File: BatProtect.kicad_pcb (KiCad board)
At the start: 2 copper layers, 94.5 x 100 mm, 57 parts, among them J1 PC104, J13 Charge3+, J16 uInv2+, J17 uInv1+, J19 uInv3+, J2 VBat1+, J3 BCharge1+, J4 BCharge3+, J5 Charge1+, J7 BCharge2+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

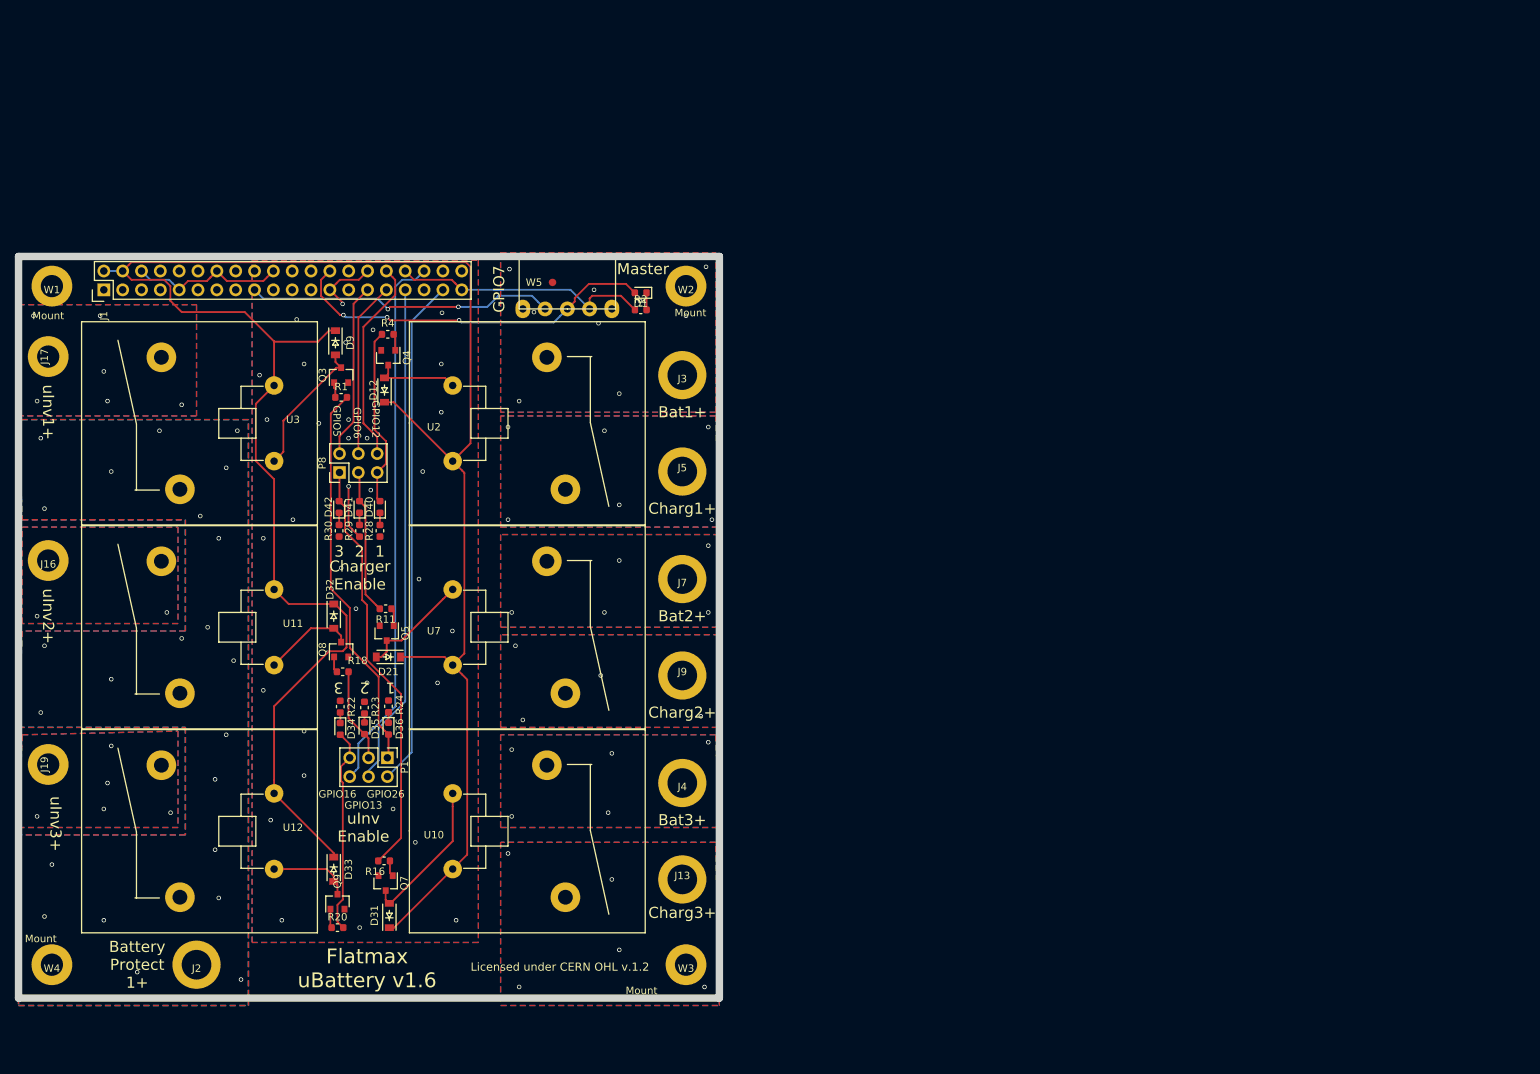
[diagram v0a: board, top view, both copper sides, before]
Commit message: Switched to the Flatmax free hardware license.
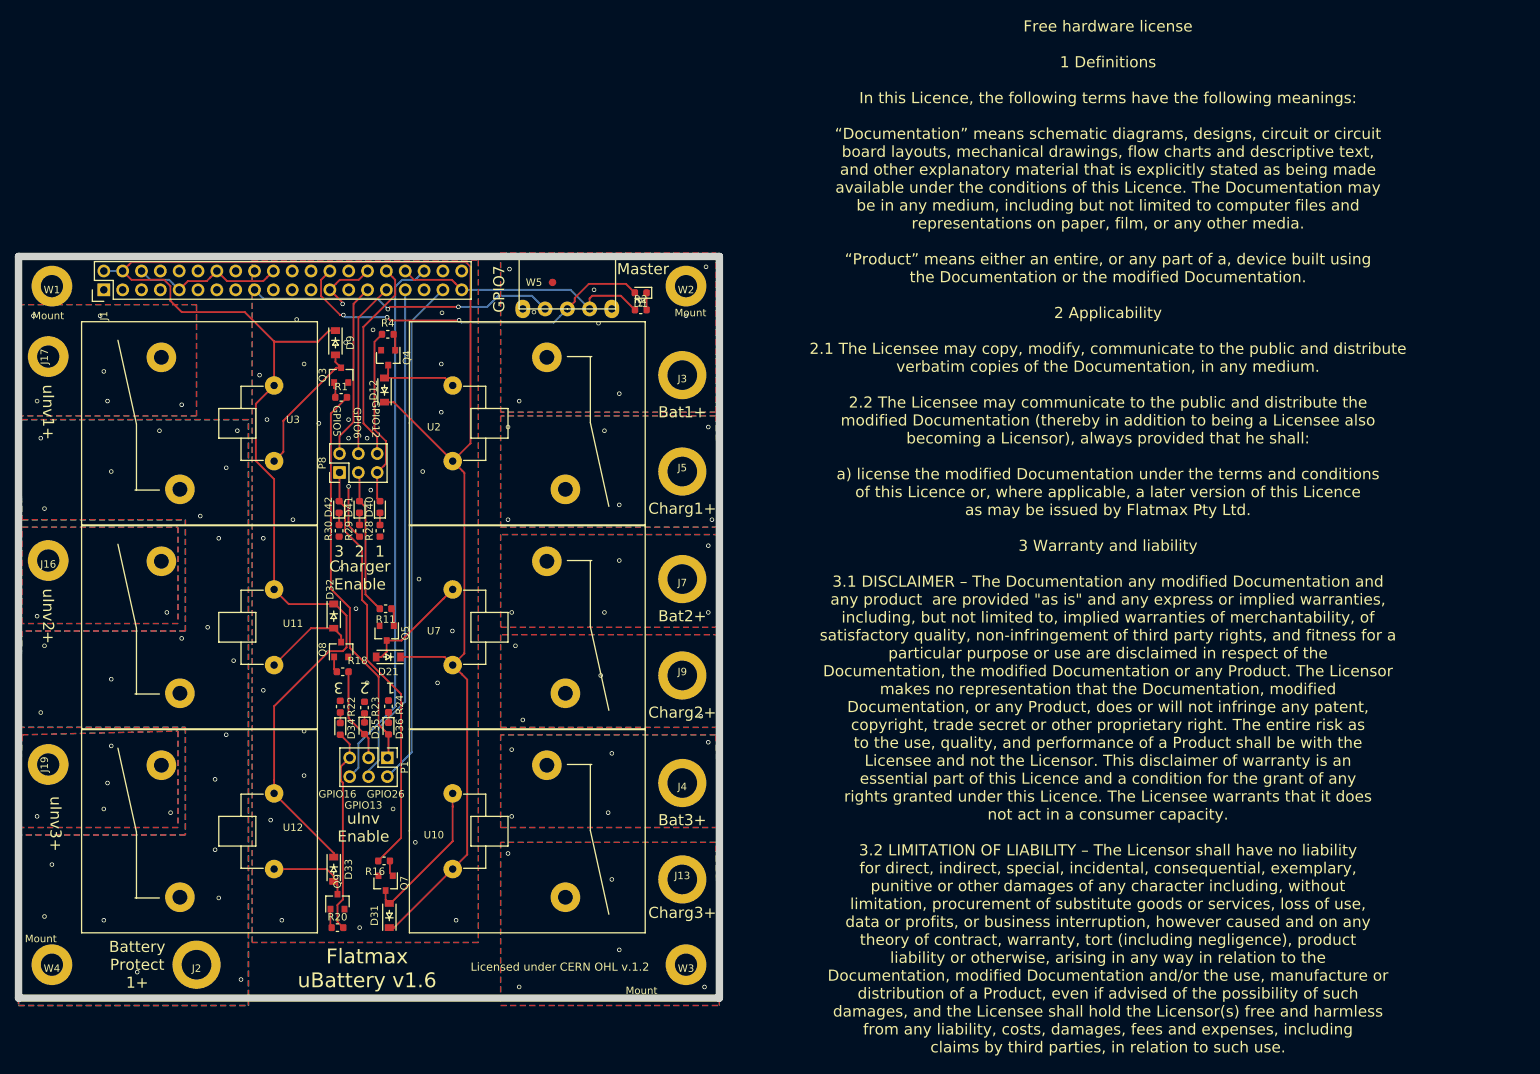
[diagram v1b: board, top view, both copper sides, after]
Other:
- board text added: "Free hardware license 1 Definitions In this Licence, the following terms have the following meanings: “Documentation” means schematic diagrams, designs, circuit or circuit board layouts, mechanical drawings, flow charts and descriptive text, and other explanatory material that is explicitly stated as being made available under the conditions of this Licence. The Documentation may be in any medium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"
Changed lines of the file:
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@@
-(kicad_pcb (version 20171130) (host pcbnew 5.0.2-bee76a0~70~ubuntu18.04.1)
+(kicad_pcb (version 20171130) (host pcbnew 5.1.4+dfsg1-1)
   (general
     (thickness 1.6)
-    (drawings 36)
+    (drawings 37)
     (tracks 349)
     (zones 0)
@@
     (zone_45_only no)
     (trace_min 0.2)
-    (segment_width 1)
-    (edge_width 0.15)
     (via_size 0.6)
     (via_drill 0.4)
@@
     (uvia_min_size 0.2)
     (uvia_min_drill 0.1)
+    (edge_width 0.15)
+    (segment_width 1)
     (pcb_text_width 0.3)
     (pcb_text_size 1.5 1.5)
@@
     )
   )
+  (gr_text "Free hardware license\n\n1 Definitions\n\nIn this Licence, the following terms have the following meanings:\n\n“Documentation” means schematic diagrams, designs, circuit or circuit\nboard layouts, mechanical drawings, flow charts and descriptive text,\nand other explanatory material that is explicitly stated as being made\navailable under the conditions of this Licence. The Documentation may\nbe in any medium, including but not limited to computer files and\nrepresentations on paper, film, or any other media.\n\n“Product” means either an entire, or any part of a, device built using\nthe Documentation or the modified Documentation.\n\n2 Applicability\n\n2.1 The Licensee may copy, modify, communicate to the public and distribute\nverbatim copies of the Documentation, in any medium.\n\n2.2 The Licensee may communicate to the public and distribute the\nmodified Documentation (thereby in addition to being a Licensee also\nbecoming a Licensor), always provided that he shall:\n\na) license the modified Documentation under the terms and conditions\nof this Licence or, where applicable, a later version of this Licence\nas may be issued by Flatmax Pty Ltd.\n\n3 Warranty and liability\n\n3.1 DISCLAIMER – The Documentation any modified Documentation and\nany product  are provided \"as is\" and any express or implied warranties,\nincluding, but not limited to, implied warranties of merchantability, of\nsatisfactory quality, non-infringement of third party rights, and fitness for a\nparticular purpose or use are disclaimed in respect of the\nDocumentation, the modified Documentation or any Product. The Licensor\nmakes no representation that the Documentation, modified\nDocumentation, or any Product, does or will not infringe any patent,\ncopyright, trade secret or other proprietary right. The entire risk as\nto the use, quality, and performance of a Product shall be with the\nLicensee and not the Licensor. This disclaimer of warranty is an\nessential part of this Licence and a condition for the grant of any\nrights granted under this Licence. The Licensee warrants that it does\nnot act in a consumer capacity.\n\n3.2 LIMITATION OF LIABILITY – The Licensor shall have no liability\nfor direct, indirect, special, incidental, consequential, exemplary,\npunitive or other damages of any character including, without\nlimitation, procurement of substitute goods or services, loss of use,\ndata or profits, or business interruption, however caused and on any\ntheory of contract, warranty, tort (including negligence), product\nliability or otherwise, arising in any way in relation to the\nDocumentation, modified Documentation and/or the use, manufacture or\ndistribution of a Product, even if advised of the possibility of such\ndamages, and the Licensee shall hold the Licensor(s) free and harmless\nfrom any liability, costs, damages, fees and expenses, including\nclaims by third parties, in relation to such use.\n" (at 204.9 100.3) (layer F.SilkS)
+    (effects (font (size 1.5 1.5) (thickness 0.3)))
+  )
   (gr_text "Licensed under CERN OHL v.1.2" (at 131 158.3) (layer F.SilkS)

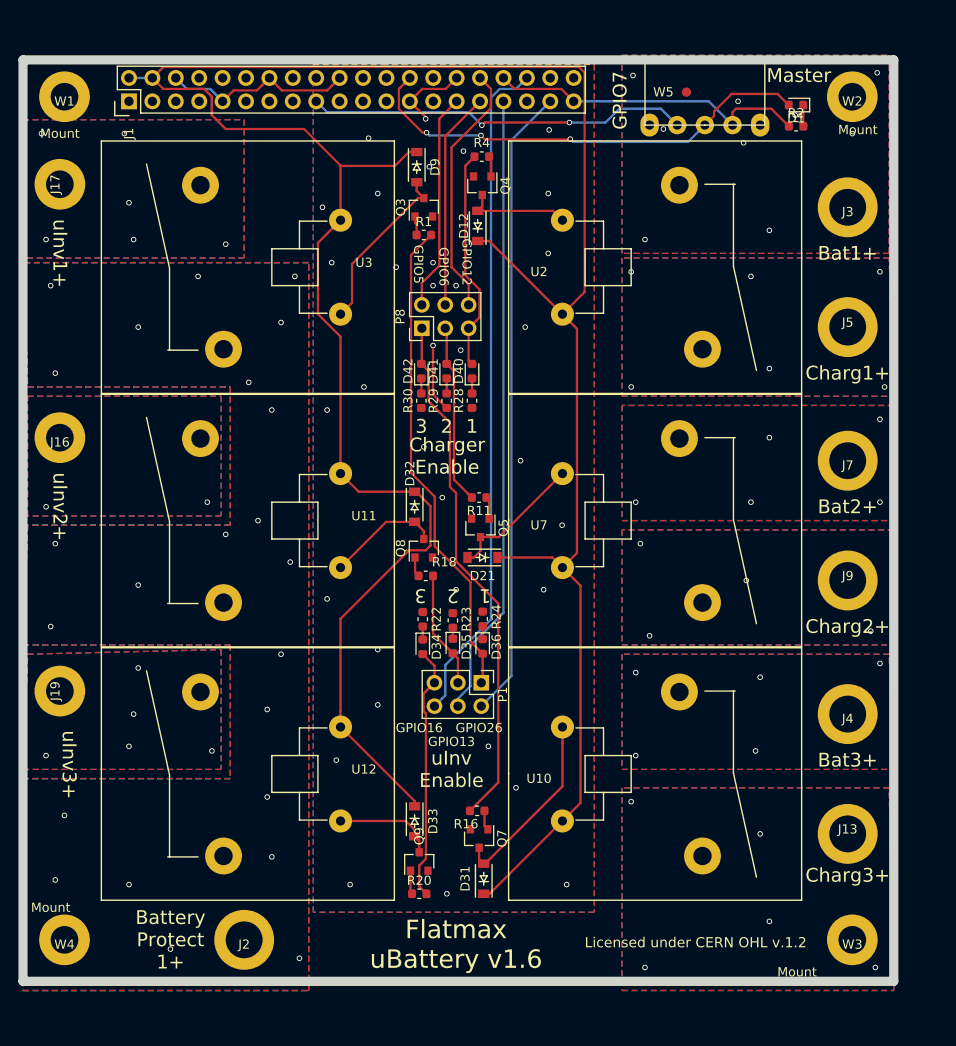
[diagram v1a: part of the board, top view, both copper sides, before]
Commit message: v2.0 Changed to AC mains relay switching.
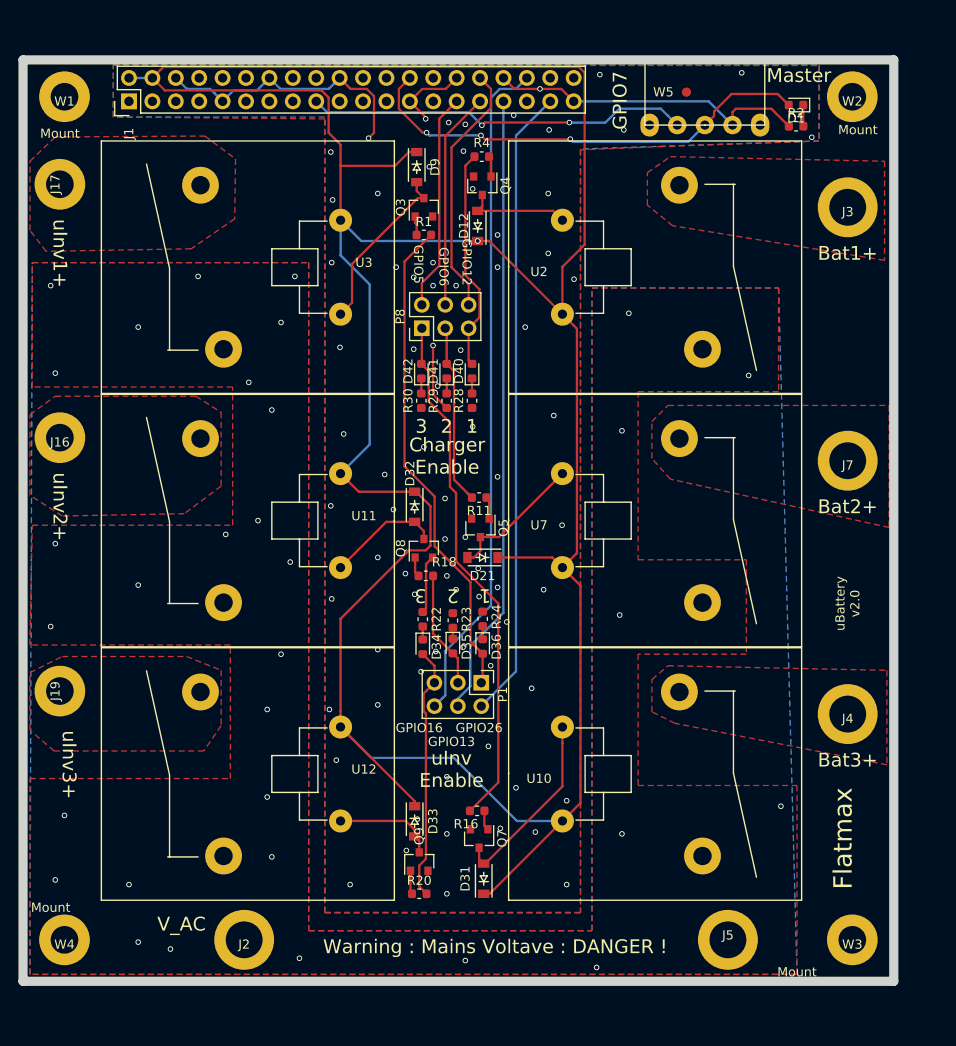
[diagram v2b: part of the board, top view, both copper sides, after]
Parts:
- removed J13: Charge3+, holes:Pin4mm
- removed J9: Charge2+, holes:Pin4mm
- J2: value VBat1+ -> VAC
- J5: value Charge1+ -> VAC
- moved J5 67.8 mm to (134.5, 158.0)
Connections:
- J2 pad 1: /uiVBat1+ -> /V_AC
- J5 pad 1: /Charger1+ -> /V_AC
- U10 pad 3: /Charger3+ -> /V_AC
- U11 pad 1: /uiVBat1+ -> /V_AC
- U12 pad 1: /uiVBat1+ -> /V_AC
- U2 pad 3: /Charger1+ -> /V_AC
- U3 pad 1: /uiVBat1+ -> /V_AC
- U7 pad 3: /Charger2+ -> /V_AC
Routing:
- net V5: track 289.3 -> 336.4 mm, vias 0 -> 1
- net DGND: track 72.6 -> 88.2 mm, vias 34 -> 76
- net /uInv1En: track 52.8 -> 53.4 mm
- net /uiVBat1+: vias 23 -> 0
- net /uInv3+: vias 5 -> 0
- net /uInv2+: vias 2 -> 0
- net /uInv1+: vias 6 -> 0
- net /V_AC: vias 0 -> 32
- net /VBat3+: vias 5 -> 0
- net /VBat2+: vias 5 -> 0
- net /VBat1+: vias 9 -> 0
- net /Charger3+: vias 5 -> 0
- net /Charger2+: vias 4 -> 0
- net /Charger1+: vias 6 -> 0
- net (no net): vias 0 -> 2
- added copper zone on B.Cu, net /V_AC
- added copper zone on F.Cu, net /V_AC
- removed copper zone on B.Cu, net /Charger1+
- removed copper zone on F.Cu, net /Charger1+
- removed copper zone on B.Cu, net /Charger2+
- removed copper zone on F.Cu, net /Charger2+
- removed copper zone on B.Cu, net /Charger3+
- removed copper zone on F.Cu, net /Charger3+
- removed copper zone on B.Cu, net /VBat1+
- removed copper zone on B.Cu, net /VBat2+
- removed copper zone on B.Cu, net /VBat3+
- removed copper zone on B.Cu, net /uInv1+
- removed copper zone on B.Cu, net /uInv2+
- removed copper zone on B.Cu, net /uInv3+
- removed copper zone on B.Cu, net /uiVBat1+
- removed copper zone on F.Cu, net /uiVBat1+
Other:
- board text added: "Flatmax"
- board text added: "V_AC"
- board text added: "Warning : Mains Voltave : DANGER !"
- board text added: "uBattery v2.0"
- board text removed: "Battery Protect 1+"
- board text removed: "Charg1+"
- board text removed: "Charg2+"
- board text removed: "Charg3+"
- board text removed: "Flatmax uBattery v1.6"
- board text removed: "Licensed under CERN OHL v.1.2"

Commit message: Switched relay names.
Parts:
- U10, U11, U12, U2, U3, U7: value SRD-105VDC-SL-A -> SLA-05VDC-SL-A
